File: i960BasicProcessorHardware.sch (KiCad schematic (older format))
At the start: 68 parts, among them J1 Conn_01x08, J10 Conn_02x39_Odd_Even, J15 Conn_01x01, J2 Conn_02x05_Odd_Even, J3 Conn_02x05_Odd_Even, J4 Conn_02x05_Odd_Even, J5 Conn_02x16_Odd_Even, J6 Conn_01x03, J7 Conn_01x03, J8 Conn_01x06, J9 Conn_01x11, U1 74HC245, U10 Adafruit_FeatherWing (PSRAM F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, U11 Adafruit_FeatherWing (PSRAM F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, U12 74LS125, U13 74LS04, U14 74LS08, U15 74LS174, U16 SN74LVC245AN, U17 74LS174, U2 80960Sx, U3 MCP23S17_SP, U4 MCP23S17_SP, U5 74HC245, U6 74HC573, U7 74HC573, U8 MCP23S17_SP, U9 MCP23S17_SP

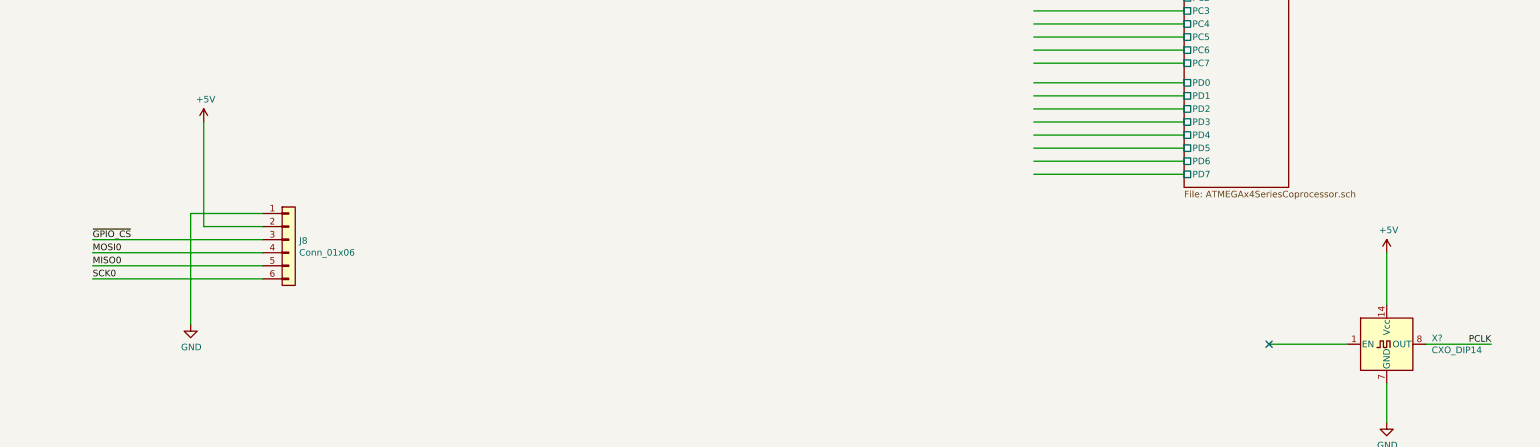
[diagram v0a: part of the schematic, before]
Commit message: Drop the extra breakout for spi
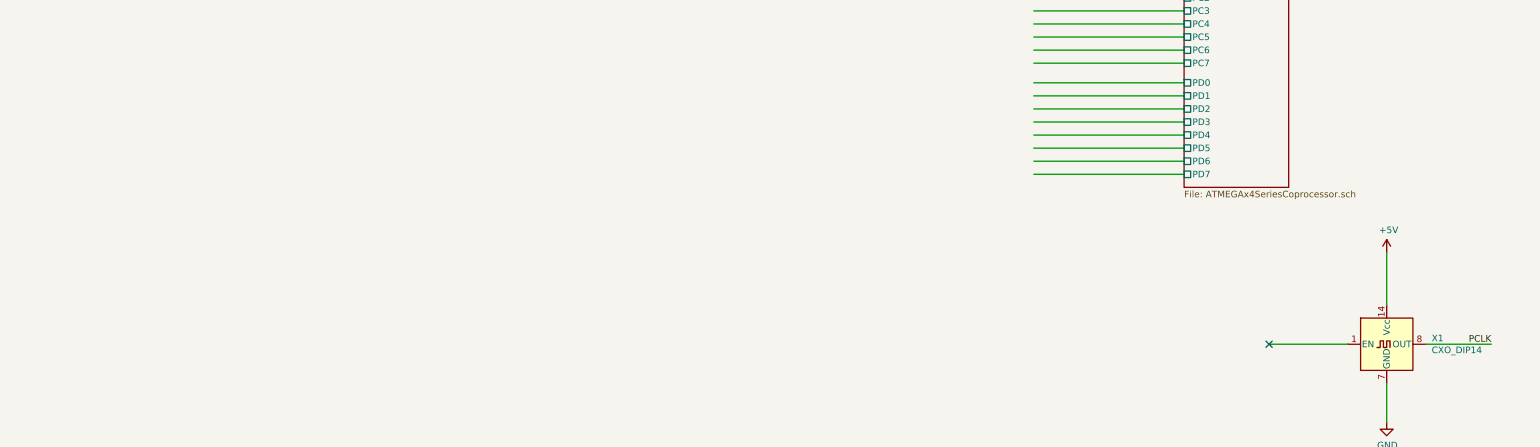
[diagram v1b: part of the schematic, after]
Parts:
- removed J8: Conn_01x06, Connector_PinHeader_2.54mm:PinHeader_1x06_P2.54mm_Vertical, symbol Connector_Generic:Conn_01x06
- gave numbers to parts that had none: 1
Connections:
- wire segments 774 -> 766
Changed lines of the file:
@@
 	1    0    0    -1
 $EndComp
-$Comp
-L Connector_Generic:Conn_01x06 J8
-U 1 1 74743549
-P 17900 5000
-F 0 "J8" H 17980 4992 50  0000 L CNN
-F 1 "Conn_01x06" H 17980 4901 50  0000 L CNN
-F 2 "Connector_PinHeader_2.54mm:PinHeader_1x06_P2.54mm_Vertical" H 17900 5000 50  0001 C CNN
-F 3 "~" H 17900 5000 50  0001 C CNN
-	1    17900 5000
-	1    0    0    -1
-$EndComp
-Wire Wire Line
-	17700 4800 17150 4800
-Wire Wire Line
-	17150 4800 17150 5650
-Wire Wire Line
-	17700 4900 17250 4900
-Wire Wire Line
-	17250 4900 17250 4100
-$Comp
-L power:+5V #PWR040
-U 1 1 74894292
-P 17250 4100
-F 0 "#PWR040" H 17250 3950 50  0001 C CNN
-F 1 "+5V" H 17265 4273 50  0000 C CNN
-F 2 "" H 17250 4100 50  0001 C CNN
-F 3 "" H 17250 4100 50  0001 C CNN
-	1    17250 4100
-	1    0    0    -1
-$EndComp
-$Comp
-L power:GND #PWR039
-U 1 1 748955E6
-P 17150 5650
-F 0 "#PWR039" H 17150 5400 50  0001 C CNN
-F 1 "GND" H 17155 5477 50  0000 C CNN
-F 2 "" H 17150 5650 50  0001 C CNN
-F 3 "" H 17150 5650 50  0001 C CNN
-	1    17150 5650
-	1    0    0    -1
-$EndComp
-Wire Wire Line
-	17700 5000 16400 5000
-Wire Wire Line
-	17700 5100 16400 5100
-Wire Wire Line
-	17700 5200 16400 5200
-Wire Wire Line
-	17700 5300 16400 5300
-Text Label 16400 5000 0    50   ~ 0
-~GPIO_CS
-Text Label 16400 5100 0    50   ~ 0
-MOSI0
-Text Label 16400 5200 0    50   ~ 0
-MISO0
-Text Label 16400 5300 0    50   ~ 0
-SCK0
 Text Label 28850 3450 0    50   ~ 0
 ~RESET960
@@
 	24750 4500 23600 4500
 $Comp
-L Oscillator:CXO_DIP14 X?
+L Oscillator:CXO_DIP14 X1
 U 1 1 7E8F4FC6
 P 26300 5800
-F 0 "X?" H 26644 5846 50  0000 L CNN
+F 0 "X1" H 26644 5846 50  0000 L CNN
 F 1 "CXO_DIP14" H 26644 5755 50  0000 L CNN
 F 2 "Oscillator:Oscillator_DIP-14" H 26750 5450 50  0001 C CNN
@@
 PCLK
 $Comp
-L power:GND #PWR?
+L power:GND #PWR0101
 U 1 1 7ECFA12B
 P 26300 6400
-F 0 "#PWR?" H 26300 6150 50  0001 C CNN
+F 0 "#PWR0101" H 26300 6150 50  0001 C CNN
 F 1 "GND" H 26305 6227 50  0000 C CNN
 F 2 "" H 26300 6400 50  0001 C CNN
@@
 P 26300 5100
 AR Path="/640CD6D6/7ECFB689" Ref="#PWR?"  Part="1"
-AR Path="/7ECFB689" Ref="#PWR?"  Part="1"
-F 0 "#PWR?" H 26300 4950 50  0001 C CNN
+AR Path="/7ECFB689" Ref="#PWR0102"  Part="1"
+F 0 "#PWR0102" H 26300 4950 50  0001 C CNN
 F 1 "+5V" H 26315 5273 50  0000 C CNN
 F 2 "" H 26300 5100 50  0001 C CNN

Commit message: Move the coprocessor clock source selector to the main page
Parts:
- added J?: Conn_01x03, Connector_PinHeader_2.54mm:PinHeader_1x03_P2.54mm_Vertical, symbol Connector_Generic:Conn_01x03
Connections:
- net labels added: EXTCLK
- wire segments 766 -> 768
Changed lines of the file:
@@
 F0 "Sheet7D8CCC79" 50
 F1 "ATMEGAx4SeriesCoprocessor.sch" 50
-F2 "SYS_CLK" I R 25550 1350 50
+F2 "CLK" I R 25550 1350 50
 F3 "AREF" O R 25550 1250 50
 F4 "PA0" U L 24750 1250 50
@@
 F35 "PD7" U L 24750 4500 50
 F36 "~SYS_RESET" I R 25550 1450 50
-F37 "PCLK" I R 25550 1550 50
 $EndSheet
 Wire Wire Line
@@
 Wire Wire Line
 	25550 1450 26650 1450
-Wire Wire Line
-	25550 1550 26650 1550
 Text Label 26650 1450 2    50   ~ 0
 ~MCU_RESET
 Text Label 26650 1350 2    50   ~ 0
-CLKO
+EXTCLK
 $Comp
 L Connector_Generic:Conn_01x01 J15
@@
 	1    0    0    -1
 $EndComp
-Text Label 26650 1550 2    50   ~ 0
-PCLK
 $Comp
 L power:+5V #PWR?
@@
 	1    0    0    -1
 $EndComp
+Wire Wire Line
+	23900 5350 23100 5350
+Text Label 23100 5350 0    50   ~ 0
+EXTCLK
+$Comp
+L Connector_Generic:Conn_01x03 J?
+U 1 1 7EDE66D8
+P 24100 5350
+AR Path="/7D8CCC7A/7EDE66D8" Ref="J?"  Part="1"
+AR Path="/7EDE66D8" Ref="J?"  Part="1"
+F 0 "J?" H 24180 5392 50  0000 L CNN
+F 1 "Conn_01x03" H 24180 5301 50  0000 L CNN
+F 2 "Connector_PinHeader_2.54mm:PinHeader_1x03_P2.54mm_Vertical" H 24100 5350 50  0001 C CNN
+F 3 "~" H 24100 5350 50  0001 C CNN
+	1    24100 5350
+	1    0    0    -1
+$EndComp
+Wire Wire Line
+	23100 5250 23900 5250
+Wire Wire Line
+	23900 5450 23100 5450
+Text Label 23100 5450 0    50   ~ 0
+PCLK
+Text Label 23100 5250 0    50   ~ 0
+CLKO
 $EndSCHEMATC

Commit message: breakout all of the coprocessor0 pins to separate headers
Bundle the AREF pin with PORTA
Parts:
- removed J15: Conn_01x01, Connector_PinHeader_2.54mm:PinHeader_1x01_P2.54mm_Vertical, symbol Connector_Generic:Conn_01x01
- added J11: Conn_01x09, symbol Connector_Generic:Conn_01x09
- added J15, J16, J17: Conn_01x08, symbol Connector_Generic:Conn_01x08
- gave numbers to parts that had none: 1
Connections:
- net labels added: COPROC0_AREF, COPROC0_PA0, COPROC0_PA1, COPROC0_PA2, COPROC0_PA3, COPROC0_PA4, COPROC0_PA5, COPROC0_PA6, COPROC0_PA7, COPROC0_PB0, COPROC0_PB1, COPROC0_PB2, COPROC0_PB3, COPROC0_PB4, COPROC0_PB5, COPROC0_PB6, COPROC0_PB7, COPROC0_PC0, COPROC0_PC1, COPROC0_PC2, COPROC0_PC3, COPROC0_PC4, COPROC0_PC5, COPROC0_PC6, COPROC0_PC7, COPROC0_PD0, COPROC0_PD1, COPROC0_PD2, COPROC0_PD3, COPROC0_PD4, COPROC0_PD5, COPROC0_PD6, COPROC0_PD7
- wire segments 768 -> 801

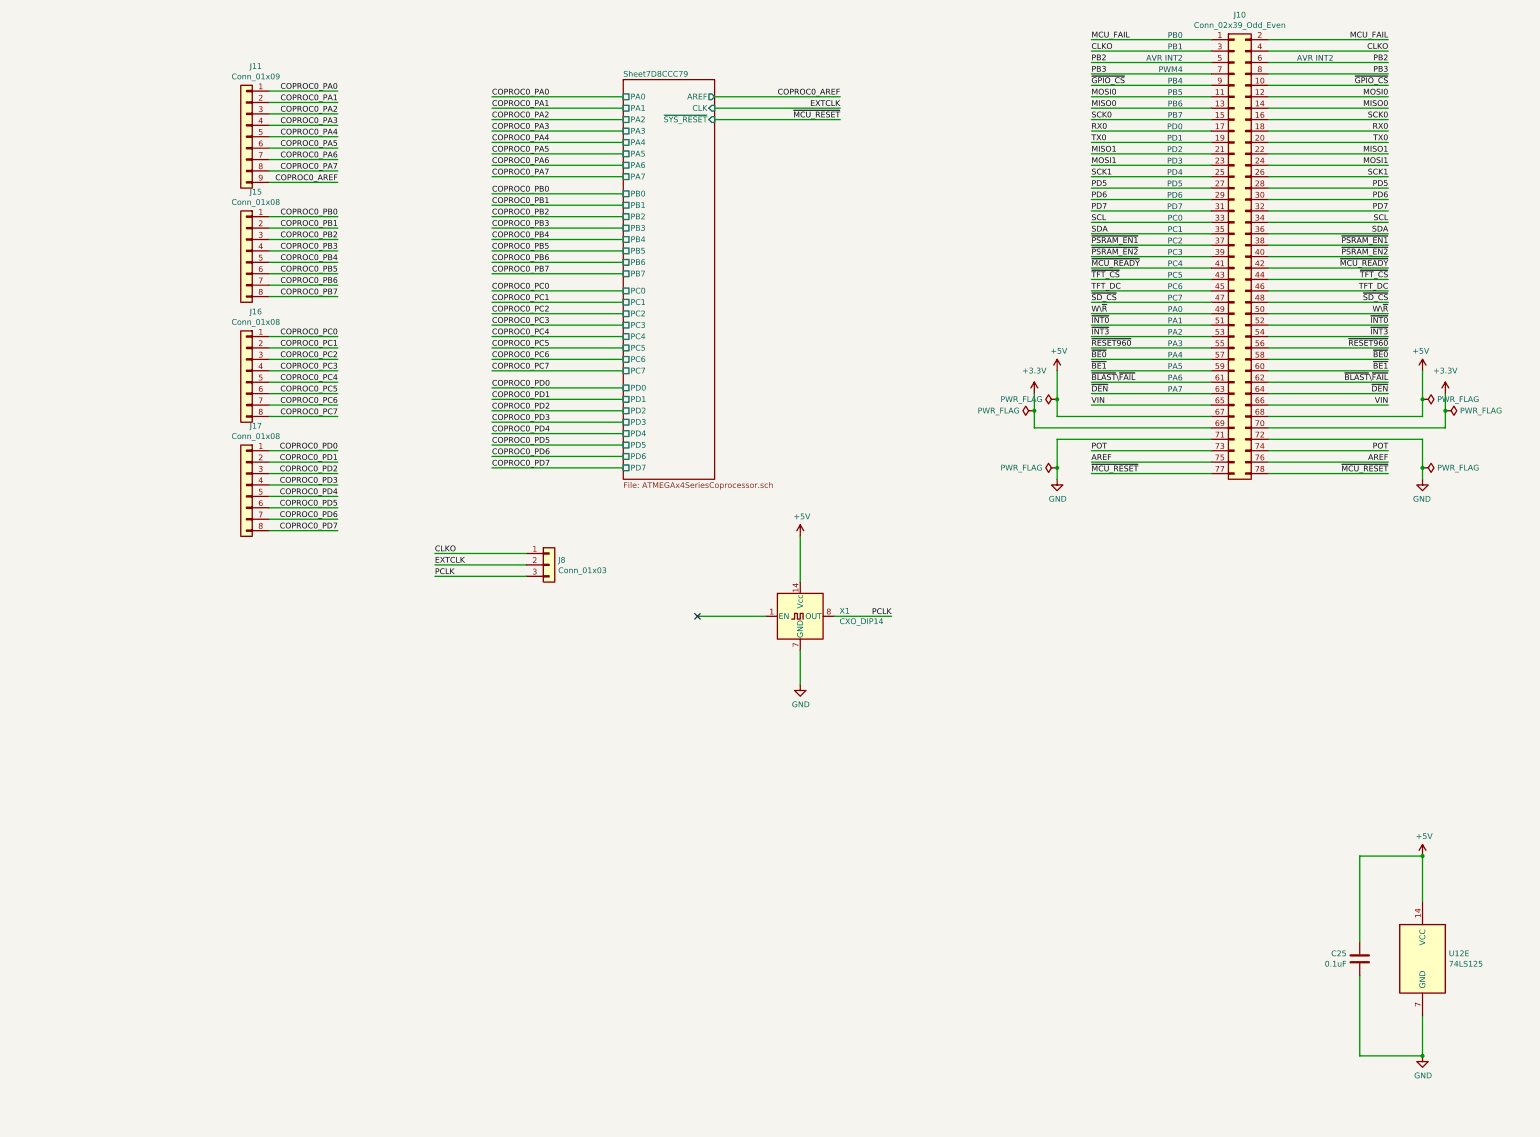
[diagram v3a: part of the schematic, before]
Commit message: Double headers for each co processor
Added a second coprocessor
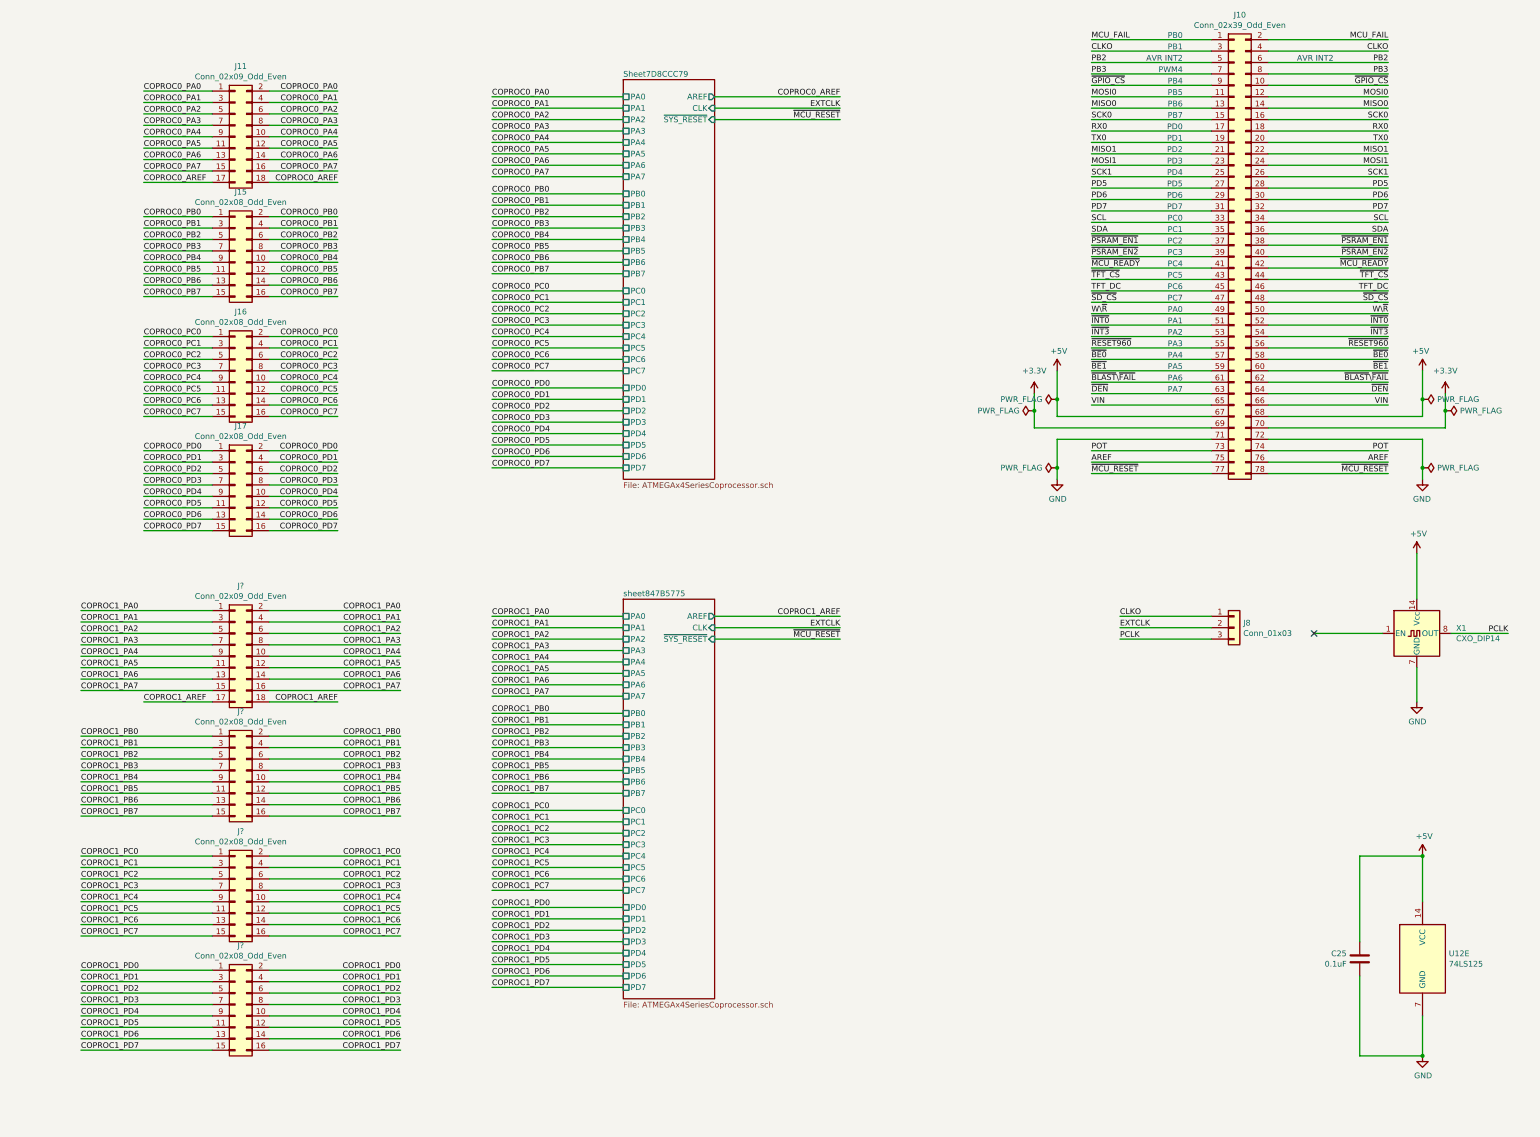
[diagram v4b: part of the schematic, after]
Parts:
- removed J11: Conn_01x09, symbol Connector_Generic:Conn_01x09
- removed J15, J16, J17: Conn_01x08, symbol Connector_Generic:Conn_01x08
- added J11, J?: Conn_02x09_Odd_Even, Connector_PinHeader_2.54mm:PinHeader_2x09_P2.54mm_Vertical, symbol Connector_Generic:Conn_02x09_Odd_Even
- added J15, J16, J17, J? (x3): Conn_02x08_Odd_Even, Connector_PinHeader_2.54mm:PinHeader_2x08_P2.54mm_Vertical, symbol Connector_Generic:Conn_02x08_Odd_Even
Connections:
- net COPROC0_AREF: now also J11.17 (Pin_17), J11.18 (Pin_18)
- net COPROC0_PA0: now also J11.1 (Pin_1), J11.2 (Pin_2)
- net COPROC0_PA1: now also J11.3 (Pin_3), J11.4 (Pin_4)
- net COPROC0_PA2: now also J11.5 (Pin_5), J11.6 (Pin_6)
- net COPROC0_PA3: now also J11.7 (Pin_7), J11.8 (Pin_8)
- net COPROC0_PA4: now also J11.10 (Pin_10), J11.9 (Pin_9)
- net COPROC0_PA5: now also J11.11 (Pin_11), J11.12 (Pin_12)
- net COPROC0_PA6: now also J11.13 (Pin_13), J11.14 (Pin_14)
- net COPROC0_PA7: now also J11.15 (Pin_15), J11.16 (Pin_16)
- net COPROC0_PB0: now also J15.1 (Pin_1), J15.2 (Pin_2)
- net COPROC0_PB1: now also J15.3 (Pin_3), J15.4 (Pin_4)
- net COPROC0_PB2: now also J15.5 (Pin_5), J15.6 (Pin_6)
- net COPROC0_PB3: now also J15.7 (Pin_7), J15.8 (Pin_8)
- net COPROC0_PB4: now also J15.10 (Pin_10), J15.9 (Pin_9)
- net COPROC0_PB5: now also J15.11 (Pin_11), J15.12 (Pin_12)
- net COPROC0_PB6: now also J15.13 (Pin_13), J15.14 (Pin_14)
- net COPROC0_PB7: now also J15.15 (Pin_15), J15.16 (Pin_16)
- net COPROC0_PC0: now also J16.1 (Pin_1), J16.2 (Pin_2)
- net COPROC0_PC1: now also J16.3 (Pin_3), J16.4 (Pin_4)
- net COPROC0_PC2: now also J16.5 (Pin_5), J16.6 (Pin_6)
- net COPROC0_PC3: now also J16.7 (Pin_7), J16.8 (Pin_8)
- net COPROC0_PC4: now also J16.10 (Pin_10), J16.9 (Pin_9)
- net COPROC0_PC5: now also J16.11 (Pin_11), J16.12 (Pin_12)
- net COPROC0_PC6: now also J16.13 (Pin_13), J16.14 (Pin_14)
- net COPROC0_PC7: now also J16.15 (Pin_15), J16.16 (Pin_16)
- net COPROC0_PD0: now also J17.1 (Pin_1), J17.2 (Pin_2)
- net COPROC0_PD1: now also J17.3 (Pin_3), J17.4 (Pin_4)
- net COPROC0_PD2: now also J17.5 (Pin_5), J17.6 (Pin_6)
- net COPROC0_PD3: now also J17.7 (Pin_7), J17.8 (Pin_8)
- net COPROC0_PD4: now also J17.10 (Pin_10), J17.9 (Pin_9)
- net COPROC0_PD5: now also J17.11 (Pin_11), J17.12 (Pin_12)
- net COPROC0_PD6: now also J17.13 (Pin_13), J17.14 (Pin_14)
- net COPROC0_PD7: now also J17.15 (Pin_15), J17.16 (Pin_16)
- new net COPROC1_AREF: J?.17 (Pin_17), J?.18 (Pin_18)
- new net COPROC1_PA0: J?.1 (Pin_1), J?.2 (Pin_2)
- new net COPROC1_PA1: J?.3 (Pin_3), J?.4 (Pin_4)
- new net COPROC1_PA2: J?.5 (Pin_5), J?.6 (Pin_6)
- new net COPROC1_PA3: J?.7 (Pin_7), J?.8 (Pin_8)
- new net COPROC1_PA4: J?.10 (Pin_10), J?.9 (Pin_9)
- new net COPROC1_PA5: J?.11 (Pin_11), J?.12 (Pin_12)
- new net COPROC1_PA6: J?.13 (Pin_13), J?.14 (Pin_14)
- new net COPROC1_PA7: J?.15 (Pin_15), J?.16 (Pin_16)
- new net COPROC1_PB0: J?.1 (Pin_1), J?.2 (Pin_2)
- new net COPROC1_PB1: J?.3 (Pin_3), J?.4 (Pin_4)
- new net COPROC1_PB2: J?.5 (Pin_5), J?.6 (Pin_6)
- new net COPROC1_PB3: J?.7 (Pin_7), J?.8 (Pin_8)
- new net COPROC1_PB4: J?.10 (Pin_10), J?.9 (Pin_9)
- new net COPROC1_PB5: J?.11 (Pin_11), J?.12 (Pin_12)
- new net COPROC1_PB6: J?.13 (Pin_13), J?.14 (Pin_14)
- new net COPROC1_PB7: J?.15 (Pin_15), J?.16 (Pin_16)
- new net COPROC1_PC0: J?.1 (Pin_1), J?.2 (Pin_2)
- new net COPROC1_PC1: J?.3 (Pin_3), J?.4 (Pin_4)
- new net COPROC1_PC2: J?.5 (Pin_5), J?.6 (Pin_6)
- new net COPROC1_PC3: J?.7 (Pin_7), J?.8 (Pin_8)
- new net COPROC1_PC4: J?.10 (Pin_10), J?.9 (Pin_9)
- new net COPROC1_PC5: J?.11 (Pin_11), J?.12 (Pin_12)
- new net COPROC1_PC6: J?.13 (Pin_13), J?.14 (Pin_14)
- new net COPROC1_PC7: J?.15 (Pin_15), J?.16 (Pin_16)
- new net COPROC1_PD0: J?.1 (Pin_1), J?.2 (Pin_2)
- new net COPROC1_PD1: J?.3 (Pin_3), J?.4 (Pin_4)
- new net COPROC1_PD2: J?.5 (Pin_5), J?.6 (Pin_6)
- new net COPROC1_PD3: J?.7 (Pin_7), J?.8 (Pin_8)
- new net COPROC1_PD4: J?.10 (Pin_10), J?.9 (Pin_9)
- new net COPROC1_PD5: J?.11 (Pin_11), J?.12 (Pin_12)
- new net COPROC1_PD6: J?.13 (Pin_13), J?.14 (Pin_14)
- new net COPROC1_PD7: J?.15 (Pin_15), J?.16 (Pin_16)
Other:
- moved on the sheet: J8, X1

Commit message: Keep futzing with the design
Added a missing +5v power source to the x4 coprocessor schematic
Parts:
- gave numbers to parts that had none: 4
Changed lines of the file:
@@
 	21650 6550 22250 6550
 $Comp
-L Connector_Generic:Conn_02x09_Odd_Even J?
+L Connector_Generic:Conn_02x09_Odd_Even J18
 U 1 1 847B5828
 P 21350 6150
-F 0 "J?" H 21400 6767 50  0000 C CNN
+F 0 "J18" H 21400 6767 50  0000 C CNN
 F 1 "Conn_02x09_Odd_Even" H 21400 6676 50  0000 C CNN
 F 2 "Connector_PinHeader_2.54mm:PinHeader_2x09_P2.54mm_Vertical" H 21350 6150 50  0001 C CNN
@@
 	21150 6550 20550 6550
 $Comp
-L Connector_Generic:Conn_02x08_Odd_Even J?
+L Connector_Generic:Conn_02x08_Odd_Even J19
 U 1 1 847B5840
 P 21350 7150
-F 0 "J?" H 21400 7667 50  0000 C CNN
+F 0 "J19" H 21400 7667 50  0000 C CNN
 F 1 "Conn_02x08_Odd_Even" H 21400 7576 50  0000 C CNN
 F 2 "Connector_PinHeader_2.54mm:PinHeader_2x08_P2.54mm_Vertical" H 21350 7150 50  0001 C CNN
@@
 $EndComp
 $Comp
-L Connector_Generic:Conn_02x08_Odd_Even J?
+L Connector_Generic:Conn_02x08_Odd_Even J20
 U 1 1 847B5846
 P 21350 8200
-F 0 "J?" H 21400 8717 50  0000 C CNN
+F 0 "J20" H 21400 8717 50  0000 C CNN
 F 1 "Conn_02x08_Odd_Even" H 21400 8626 50  0000 C CNN
 F 2 "Connector_PinHeader_2.54mm:PinHeader_2x08_P2.54mm_Vertical" H 21350 8200 50  0001 C CNN
@@
 $EndComp
 $Comp
-L Connector_Generic:Conn_02x08_Odd_Even J?
+L Connector_Generic:Conn_02x08_Odd_Even J21
 U 1 1 847B584C
 P 21350 9200
-F 0 "J?" H 21400 9717 50  0000 C CNN
+F 0 "J21" H 21400 9717 50  0000 C CNN
 F 1 "Conn_02x08_Odd_Even" H 21400 9626 50  0000 C CNN
 F 2 "Connector_PinHeader_2.54mm:PinHeader_2x08_P2.54mm_Vertical" H 21350 9200 50  0001 C CNN

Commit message: Rudimentary layout
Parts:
- removed J19, J21: Conn_02x08_Odd_Even, Connector_PinHeader_2.54mm:PinHeader_2x08_P2.54mm_Vertical, symbol Connector_Generic:Conn_02x08_Odd_Even
- added J?: Conn_02x16_Odd_Even, Connector_PinHeader_2.54mm:PinHeader_2x16_P2.54mm_Vertical, symbol Connector_Generic:Conn_02x16_Odd_Even
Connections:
- net COPROC1_PB0: now also J?.1 (Pin_1), J?.2 (Pin_2)
- net COPROC1_PB1: now also J?.3 (Pin_3), J?.4 (Pin_4)
- net COPROC1_PB2: now also J?.5 (Pin_5), J?.6 (Pin_6)
- net COPROC1_PB3: now also J?.7 (Pin_7), J?.8 (Pin_8)
- net COPROC1_PB4: now also J?.10 (Pin_10), J?.9 (Pin_9)
- net COPROC1_PB5: now also J?.11 (Pin_11), J?.12 (Pin_12)
- net COPROC1_PB6: now also J?.13 (Pin_13), J?.14 (Pin_14)
- net COPROC1_PB7: now also J?.15 (Pin_15), J?.16 (Pin_16)
- net COPROC1_PD0: now also J?.17 (Pin_17), J?.18 (Pin_18)
- net COPROC1_PD1: now also J?.19 (Pin_19), J?.20 (Pin_20)
- net COPROC1_PD2: now also J?.21 (Pin_21), J?.22 (Pin_22)
- net COPROC1_PD3: now also J?.23 (Pin_23), J?.24 (Pin_24)
- net COPROC1_PD4: now also J?.25 (Pin_25), J?.26 (Pin_26)
- net COPROC1_PD5: now also J?.27 (Pin_27), J?.28 (Pin_28)
- net COPROC1_PD6: now also J?.29 (Pin_29), J?.30 (Pin_30)
- net COPROC1_PD7: now also J?.31 (Pin_31), J?.32 (Pin_32)
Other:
- moved on the sheet: J20
